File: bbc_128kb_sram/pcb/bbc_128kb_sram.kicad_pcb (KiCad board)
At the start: 2 copper layers, 35.9 x 38 mm, 10 parts, among them U1 74HCT00

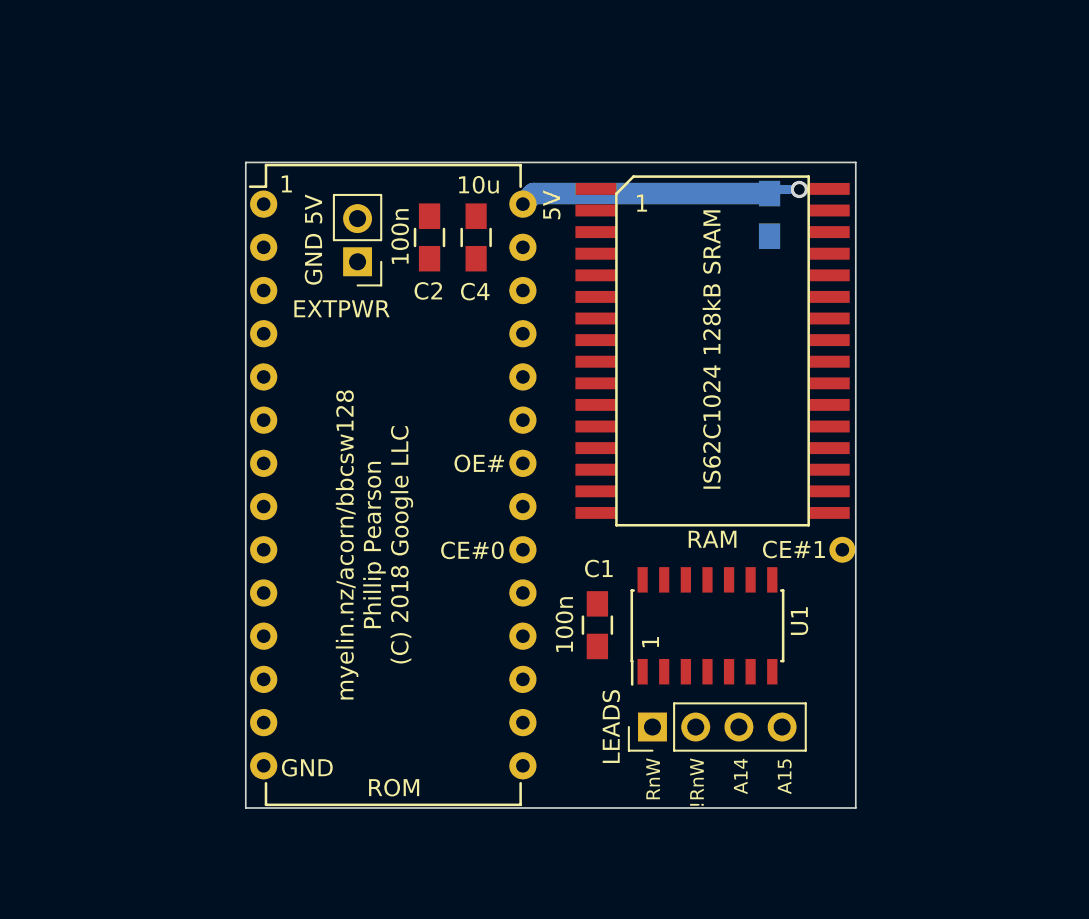
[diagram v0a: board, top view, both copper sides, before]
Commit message: Mostly routed.  Working out the quad NAND logic now.
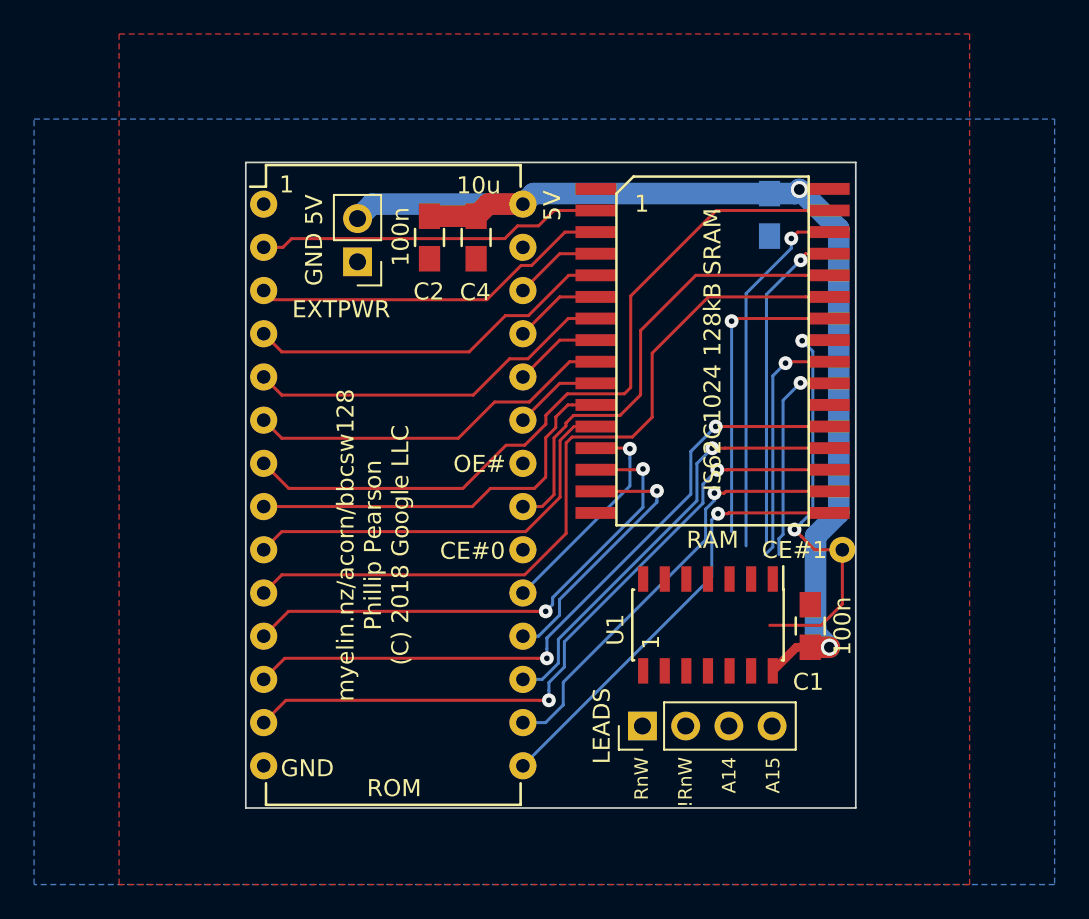
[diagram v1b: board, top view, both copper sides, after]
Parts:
- moved C1 12.5 mm to (180.6, 129.8), turned to 90 degrees
- moved LEADS 0.59 mm to (170.8, 135.7)
- moved U1 0.06 mm to (174.6, 129.7), turned to 270 degrees
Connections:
- RAM pad 10: A2 -> A11
- RAM pad 11: A1 -> A2
- RAM pad 12: A0 -> A1
- RAM pad 14: D5 -> D0
- RAM pad 15: D0 -> D6
- RAM pad 17: D1 -> D3
- RAM pad 18: D2 -> D4
- RAM pad 19: D4 -> D2
- RAM pad 2: A11 -> A12
- RAM pad 20: D6 -> D5
- RAM pad 21: D3 -> D1
- RAM pad 25: A16 -> bbc_nCS1
- RAM pad 27: A7 -> A0
- RAM pad 28: A13 -> A10
- RAM pad 3: A8 -> A7
- RAM pad 31: A10 -> A3
- RAM pad 4: A9 -> A13
- RAM pad 5: A12 -> A6
- RAM pad 6: A6 -> A8
- RAM pad 8: A4 -> A9
- RAM pad 9: A3 -> A4
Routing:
- net 5V: track 18.4 -> 66.9 mm, vias 1 -> 2
- net A0: track 0.00 -> 45.8 mm
- net A3: track 0.00 -> 44.1 mm
- net D1: track 0.00 -> 41.6 mm, vias 0 -> 2
- net D2: track 0.00 -> 41.5 mm, vias 0 -> 2
- net D0: track 0.00 -> 30.7 mm, vias 0 -> 2
- net A10: track 0.00 -> 27.9 mm
- net D3: track 0.00 -> 26.1 mm, vias 0 -> 1
- net D5: track 0.00 -> 25.7 mm, vias 0 -> 1
- net D4: track 0.00 -> 25.7 mm, vias 0 -> 1
- net bbc_nCS1: track 0.00 -> 24.7 mm, vias 0 -> 2
- net A1: track 0.00 -> 24.5 mm
- net A2: track 0.00 -> 23.7 mm
- net sram_CE: track 0.00 -> 22.4 mm, vias 0 -> 1
- net A7: track 0.00 -> 22.3 mm
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- added copper zone on B.Cu, net GND
- added copper zone on F.Cu, net GND
